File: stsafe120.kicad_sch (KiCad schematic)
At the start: 5 parts, among them U7 STSAFA120DFSPL05

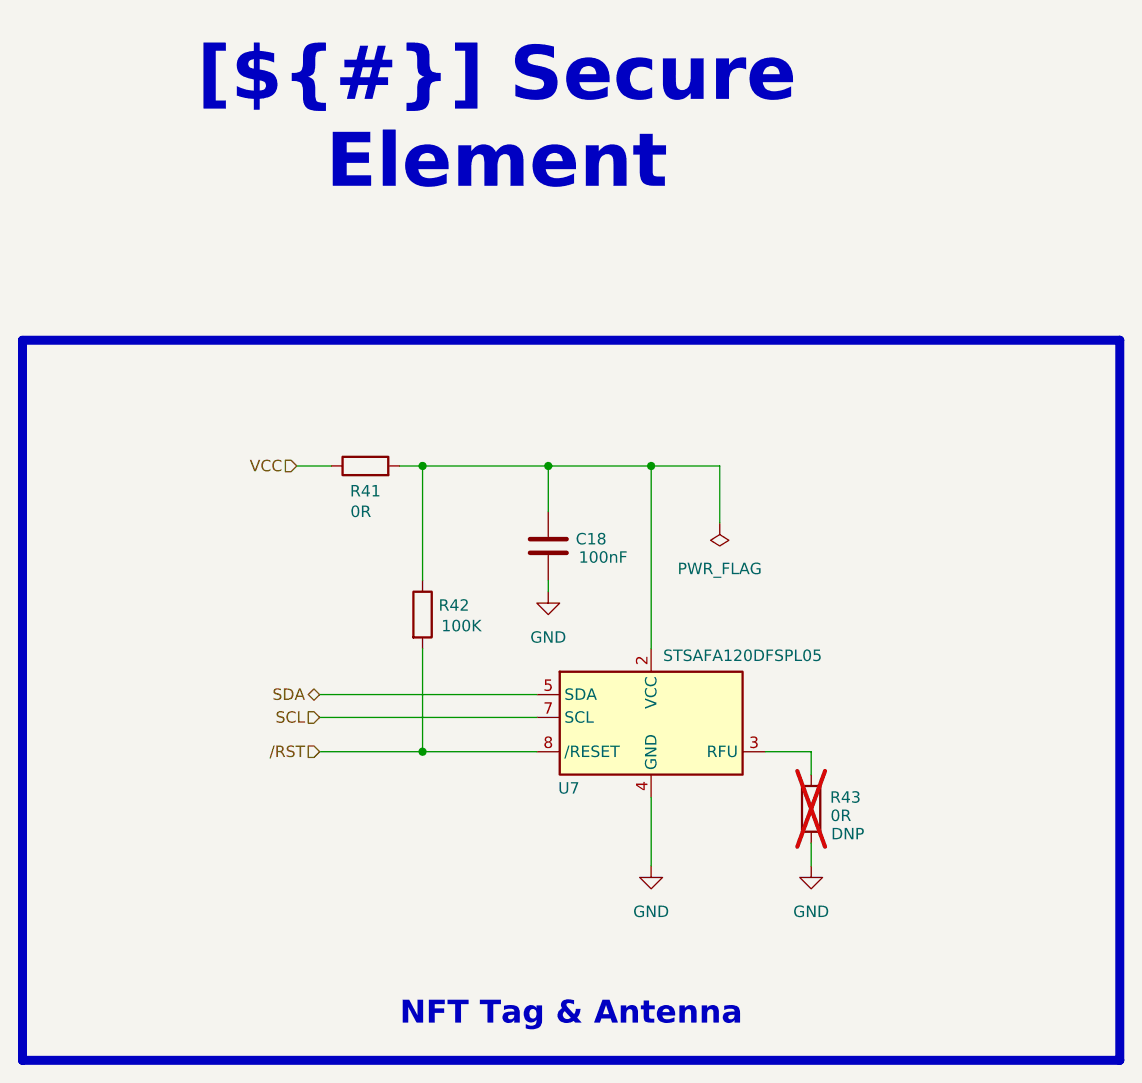
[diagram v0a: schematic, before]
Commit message: fix(hardware): replace jumper/passive footprints with 0402 and refine schematics
- Replace 0-ohm jumper resistors with 0402 package equivalents
- Reduce package size on several capacitors
- Correct and simplify several schematic symbols (replaced with
  simplified equivalents where the original was overcomplicated)
- Bump lib submodule to the updated component library (renamed
  switch footprints, new Conn_01x02_MountingPin symbol, pad/pin
  numbering fixes, approved IPN assignments, Workart artwork library)
- Register Workart.pretty in fp-lib-table
- Mark J3 as DNP in mcu.kicad_sch
- Continue schematic wiring/placement (Leds.kicad_sch, tessera.kicad_sch)
  and PCB routing/placement (tessera.kicad_pcb)
- Add board outline source (Images/pcb_size.dxf, pcb_shape.FCStd) and
  silkscreen artwork sources (Logos/) for the Workart footprints
- Complete preliminary version of PCB
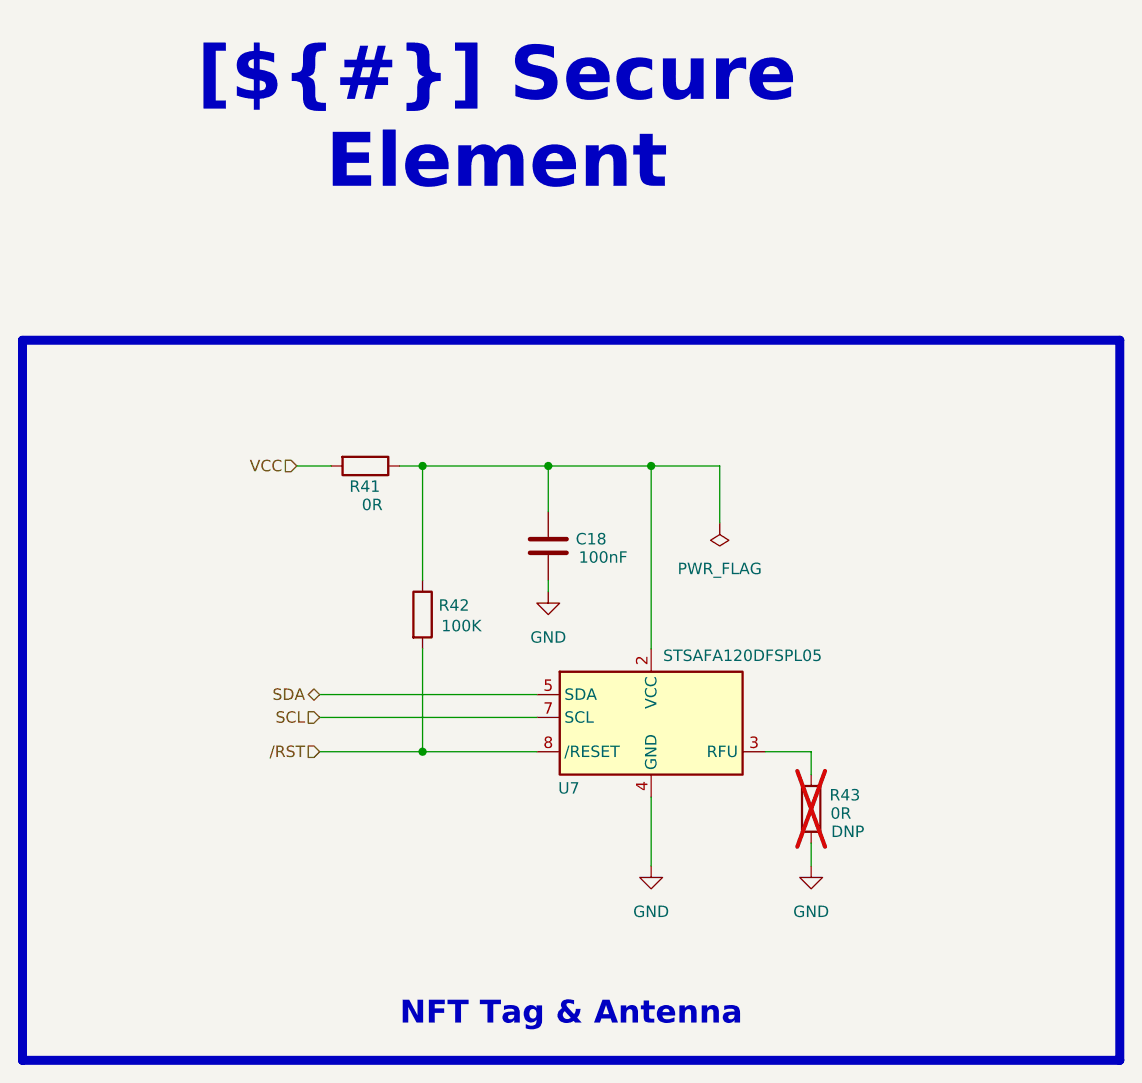
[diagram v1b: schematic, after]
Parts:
- removed R41, R43: 0R ±5% 1/10W, Resistor_SMD:R_0603_1608Metric, symbol catalog:Resistors/R0603_0R_0.1W_±5%
- added R41, R43: 0R ±5% 1/16W, Resistor_SMD:R_0402_1005Metric, symbol catalog:Resistors/R0402_0R_0.1W_±5%
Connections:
- net GND: now also U7.9 (EP), R43.2
- net VCC: now also R41.2
- net at C18.1, R42.1, U7.2 (VCC): now also R41.1
- net at U7.3 (RFU): now also R43.1
